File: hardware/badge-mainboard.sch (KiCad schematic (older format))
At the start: 35 parts, among them J1 Vin, J2 Vin, J3 Rpi_02x20_WaveShareEPD, J4 I2C_HEADER, J5 I2C_HEADER, SW1 User Button 2, SW2 User Button 1, SW3 User Button 3, SW4 User Button 4, U1 LM1117-3.3, U2 sensor-module-board

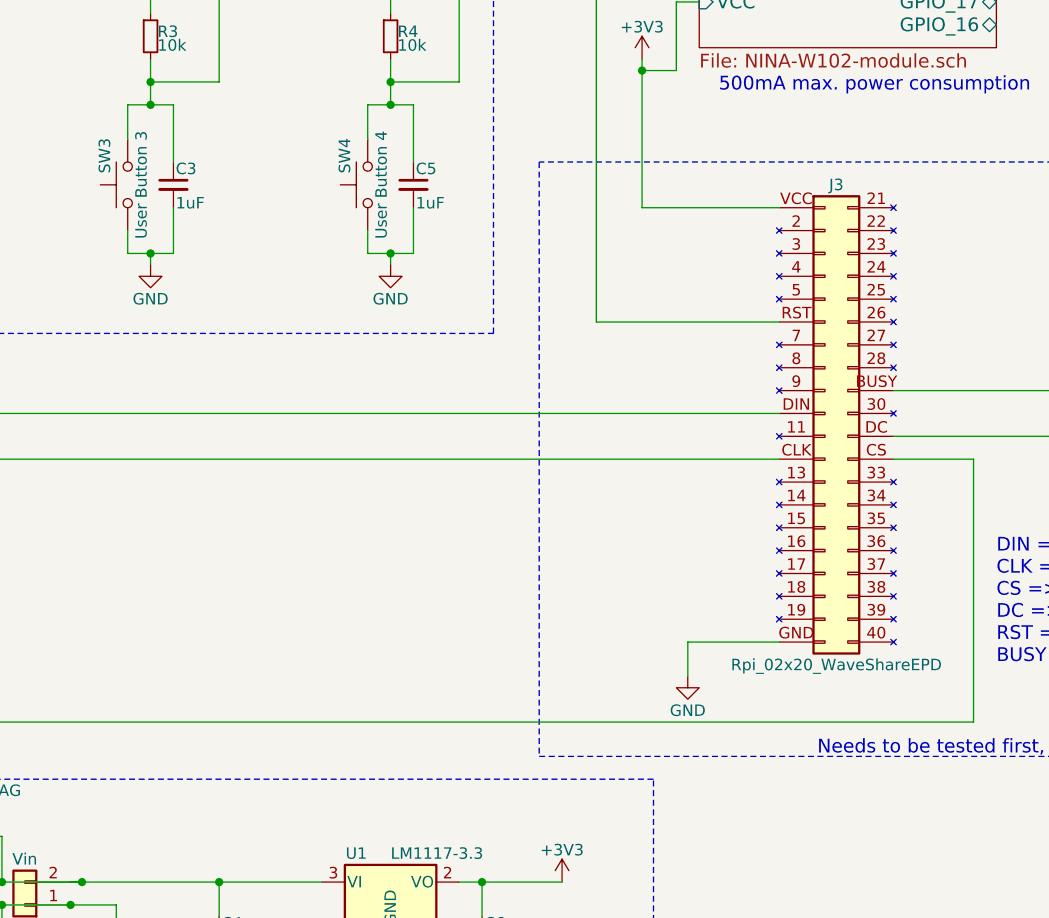
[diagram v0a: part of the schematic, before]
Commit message: Added some placement comments for the EPD to ensure orientation
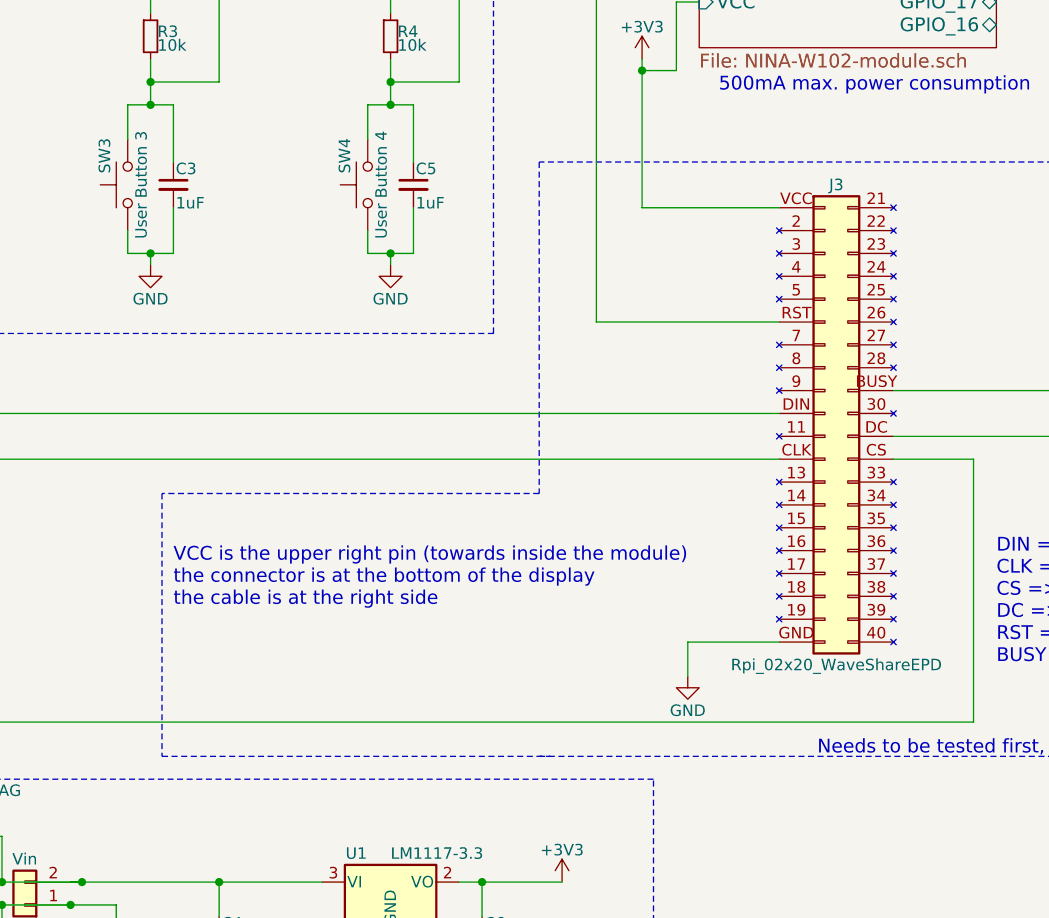
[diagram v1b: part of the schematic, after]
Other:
- note added: "VCC is the upper right pin (towards inside the module)\nthe connector is at the bottom of the display\nthe cable is at the right side"
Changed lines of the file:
@@
 	4750 5850 4750 6000
-Wire Notes Line
-	4100 3750 4100 6350
 Wire Notes Line
 	4100 6350 8700 6350
@@
 	4750 1250 4750 1200
 Connection ~ 4750 1200
+Text Notes 2500 5700 0    60   ~ 0
+VCC is the upper right pin (towards inside the module)\nthe connector is at the bottom of the display\nthe cable is at the right side
+Wire Notes Line
+	4100 5200 2450 5200
+Wire Notes Line
+	2450 5200 2450 6350
+Wire Notes Line
+	2450 6350 4150 6350
+Wire Notes Line
+	4100 3750 4100 5200
 $EndSCHEMATC

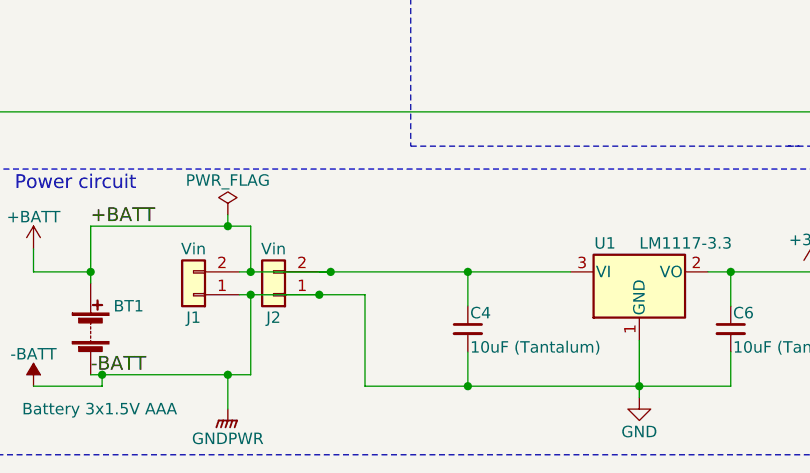
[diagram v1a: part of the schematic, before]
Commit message: removed duplicated battery terminal
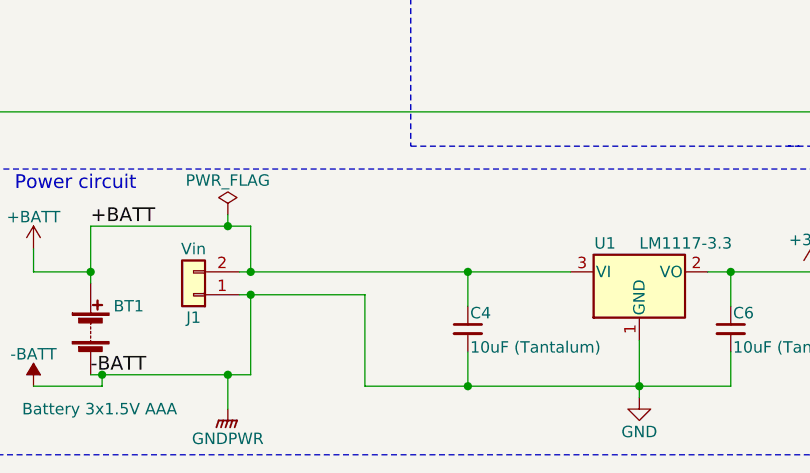
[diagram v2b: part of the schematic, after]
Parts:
- removed J2: Vin, symbol Conn_01x02
- BT1: footprint (none) -> Battery_Holders:Keystone_2479_3xAAA
- C1, C2, C3, C4, C5, C6, C7, C8, C9: footprint (none) -> Capacitors_SMD:C_1206
- D1: footprint (none) -> Diodes_SMD:D_SOD-123
- J1: footprint (none) -> Connectors-SparkFun:1X02_LOCK_LONGPADS
- J3: footprint (none) -> Connectors-SparkFun:2X20_NOSILK
- J4, J5: footprint (none) -> Connectors-SparkFun:1X04_LOCK_LONGPADS
- JP1: footprint SMT-JUMPER_2_NC -> lib:SMT-JUMPER_2_NC_TRACE_SILK
- LED1, LED2: footprint WS2812B_1 -> LED:WS2812B
- R1, R10, R2, R3, R4, R5, R6, R9: footprint (none) -> Resistors_SMD:R_1206
- R7, R8: footprint (none) -> Resistors_SMD:R_1206_HandSoldering
- SW1, SW2, SW3, SW4: footprint (none) -> switches:TACTILE_SWITCH_SMD_6.0X6.0MM
- U1: footprint (none) -> digikey-footprints:SOT-223
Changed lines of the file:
@@
 Title "IoT conference badge - mainboard"
 Date "2018-05-20"
-Rev "0.3.4"
+Rev "0.3.5"
 Comp "MakeZürich (makezurich.ch) & GDG Zürich (gdgzh.ch)"
 Comment1 ""
@@
 F 0 "LED1" H 10550 4300 50  0000 L CNN
 F 1 "WS2812b" H 10550 4200 50  0000 L CNN
-F 2 "WS2812B_1" H 10550 4100 50  0001 L CNN
+F 2 "LED:WS2812B" H 10550 4100 50  0001 L CNN
 F 3 "http://www.adafruit.com/datasheets/WS2812B.pdf" H 10550 4000 50  0001 L CNN
 F 4 "Intelligent control LED integrated light source, 4-pin SMD" H 10550 3900 50  0001 L CNN "Description"
@@
 F 0 "R5" H 7830 720 50  0000 L CNN
 F 1 "4.7k" H 7830 660 50  0000 L CNN
-F 2 "" H 7800 700 50  0001 C CNN
+F 2 "Resistors_SMD:R_1206" H 7800 700 50  0001 C CNN
 F 3 "" H 7800 700 50  0001 C CNN
 	1    7800 700
@@
 F 0 "C8" H 9360 4270 50  0000 L CNN
 F 1 "100nF" H 9360 4120 50  0000 L CNN
-F 2 "" H 9350 4200 50  0001 C CNN
+F 2 "Capacitors_SMD:C_1206" H 9350 4200 50  0001 C CNN
 F 3 "" H 9350 4200 50  0001 C CNN
 	1    9350 4200
@@
 F 0 "C9" H 9360 4920 50  0000 L CNN
 F 1 "100nF" H 9360 4770 50  0000 L CNN
-F 2 "" H 9350 4850 50  0001 C CNN
+F 2 "Capacitors_SMD:C_1206" H 9350 4850 50  0001 C CNN
 F 3 "" H 9350 4850 50  0001 C CNN
 	1    9350 4850
@@
 F 0 "C7" H 8960 4020 50  0000 L CNN
 F 1 "47uF" H 8960 3870 50  0000 L CNN
-F 2 "" H 8950 3950 50  0001 C CNN
+F 2 "Capacitors_SMD:C_1206" H 8950 3950 50  0001 C CNN
 F 3 "" H 8950 3950 50  0001 C CNN
 	1    8950 3950
@@
 F 0 "R6" H 7830 1270 50  0000 L CNN
 F 1 "4.7k" H 7830 1210 50  0000 L CNN
-F 2 "" H 7800 1250 50  0001 C CNN
+F 2 "Resistors_SMD:R_1206" H 7800 1250 50  0001 C CNN
 F 3 "" H 7800 1250 50  0001 C CNN
 	1    7800 1250
@@
 F 0 "J4" H 9250 2250 50  0000 C CNN
 F 1 "I2C_HEADER" H 9250 1750 50  0000 C CNN
-F 2 "" H 9250 2050 50  0001 C CNN
+F 2 "Connectors-SparkFun:1X04_LOCK_LONGPADS" H 9250 2050 50  0001 C CNN
 F 3 "" H 9250 2050 50  0001 C CNN
 	1    9250 2050
@@
 F 0 "J5" H 9800 2250 50  0000 C CNN
 F 1 "I2C_HEADER" H 9800 1750 50  0000 C CNN
-F 2 "" H 9800 2050 50  0001 C CNN
+F 2 "Connectors-SparkFun:1X04_LOCK_LONGPADS" H 9800 2050 50  0001 C CNN
 F 3 "" H 9800 2050 50  0001 C CNN
 	1    9800 2050
@@
 F 0 "R7" H 7830 1820 50  0000 L CNN
 F 1 "4.7k" H 7830 1760 50  0000 L CNN
-F 2 "" H 7800 1800 50  0001 C CNN
+F 2 "Resistors_SMD:R_1206_HandSoldering" H 7800 1800 50  0001 C CNN
 F 3 "" H 7800 1800 50  0001 C CNN
 	1    7800 1800
@@
 F 0 "R8" H 8180 1820 50  0000 L CNN
 F 1 "4.7k" H 8180 1760 50  0000 L CNN
-F 2 "" H 8150 1800 50  0001 C CNN
+F 2 "Resistors_SMD:R_1206_HandSoldering" H 8150 1800 50  0001 C CNN
 F 3 "" H 8150 1800 50  0001 C CNN
 	1    8150 1800
@@
 F 0 "U1" H 3300 7025 50  0000 C CNN
 F 1 "LM1117-3.3" H 3450 7025 50  0000 L CNN
-F 2 "" H 3450 6900 50  0001 C CNN
+F 2 "digikey-footprints:SOT-223" H 3450 6900 50  0001 C CNN
 F 3 "" H 3450 6900 50  0001 C CNN
 	1    3450 6900
@@
 F 0 "C4" H 2710 7220 50  0000 L CNN
 F 1 "10uF (Tantalum)" H 2710 7070 50  0000 L CNN
-F 2 "" H 2700 7150 50  0001 C CNN
+F 2 "Capacitors_SMD:C_1206" H 2700 7150 50  0001 C CNN
 F 3 "" H 2700 7150 50  0001 C CNN
 	1    2700 7150
@@
 F 0 "C6" H 3860 7220 50  0000 L CNN
 F 1 "10uF (Tantalum)" H 3860 7070 50  0000 L CNN
-F 2 "" H 3850 7150 50  0001 C CNN
+F 2 "Capacitors_SMD:C_1206" H 3850 7150 50  0001 C CNN
 F 3 "" H 3850 7150 50  0001 C CNN
 	1    3850 7150
@@
 $EndComp
 $Comp
-L Conn_01x02 J2
-U 1 1 5B02ACC9
-P 1850 7000
-F 0 "J2" H 1850 7100 50  0000 C CNN
-F 1 "Vin" H 1850 6800 50  0000 C CNN
-F 2 "" H 1850 7000 50  0001 C CNN
-F 3 "" H 1850 7000 50  0001 C CNN
-	1    1850 7000
-	-1   0    0    1
-$EndComp
-$Comp
 L Battery BT1
 U 1 1 5B02C983
@@
 F 0 "BT1" H 1150 7250 50  0000 L CNN
 F 1 "Battery 3x1.5V AAA" H 750 6800 50  0000 L CNN
-F 2 "" V 1050 7210 50  0001 C CNN
+F 2 "Battery_Holders:Keystone_2479_3xAAA" V 1050 7210 50  0001 C CNN
 F 3 "" V 1050 7210 50  0001 C CNN
 	1    1050 7150
@@
 F 0 "J1" H 1500 7100 50  0000 C CNN
 F 1 "Vin" H 1500 6800 50  0000 C CNN
-F 2 "" H 1500 7000 50  0001 C CNN
+F 2 "Connectors-SparkFun:1X02_LOCK_LONGPADS" H 1500 7000 50  0001 C CNN
 F 3 "" H 1500 7000 50  0001 C CNN
 	1    1500 7000
@@
 F 0 "LED2" H 10550 4900 50  0000 L CNN
 F 1 "WS2812b" H 10550 4800 50  0000 L CNN
-F 2 "WS2812B_1" H 10550 4700 50  0001 L CNN
+F 2 "LED:WS2812B" H 10550 4700 50  0001 L CNN
 F 3 "http://www.adafruit.com/datasheets/WS2812B.pdf" H 10550 4600 50  0001 L CNN
 F 4 "Intelligent control LED integrated light source, 4-pin SMD" H 10550 4500 50  0001 L CNN "Description"
@@
 F 0 "J3" H 5400 5850 50  0000 C CNN
 F 1 "Rpi_02x20_WaveShareEPD" H 5400 3750 50  0000 C CNN
-F 2 "" H 5350 4850 50  0001 C CNN
+F 2 "Connectors-SparkFun:2X20_NOSILK" H 5350 4850 50  0001 C CNN
 F 3 "" H 5350 4850 50  0001 C CNN
 	1    5350 4850
@@
 F 0 "SW2" H 1650 1700 50  0000 L CNN
 F 1 "User Button 1" H 1600 1540 50  0000 C CNN
-F 2 "" H 1600 1800 50  0001 C CNN
+F 2 "switches:TACTILE_SWITCH_SMD_6.0X6.0MM" H 1600 1800 50  0001 C CNN
 F 3 "" H 1600 1800 50  0001 C CNN
 	1    1600 1600
@@
 F 0 "C2" H 1810 1670 50  0000 L CNN
 F 1 "1uF" H 1810 1520 50  0000 L CNN
-F 2 "" H 1800 1600 50  0001 C CNN
+F 2 "Capacitors_SMD:C_1206" H 1800 1600 50  0001 C CNN
 F 3 "" H 1800 1600 50  0001 C CNN
 	1    1800 1600
@@
 F 0 "R2" H 1730 970 50  0000 L CNN
 F 1 "10k" H 1730 910 50  0000 L CNN
-F 2 "" H 1700 950 50  0001 C CNN
+F 2 "Resistors_SMD:R_1206" H 1700 950 50  0001 C CNN
 F 3 "" H 1700 950 50  0001 C CNN
 	1    1700 950
@@
 F 0 "SW1" H 1350 3950 50  0000 L CNN
 F 1 "User Button 2" H 1300 3790 50  0000 C CNN
-F 2 "" H 1300 4050 50  0001 C CNN
+F 2 "switches:TACTILE_SWITCH_SMD_6.0X6.0MM" H 1300 4050 50  0001 C CNN
 F 3 "" H 1300 4050 50  0001 C CNN
 	1    1300 3850
@@
 F 0 "C1" H 1510 3920 50  0000 L CNN
 F 1 "1uF" H 1510 3770 50  0000 L CNN
-F 2 "" H 1500 3850 50  0001 C CNN
+F 2 "Capacitors_SMD:C_1206" H 1500 3850 50  0001 C CNN
 F 3 "" H 1500 3850 50  0001 C CNN
 	1    1500 3850
@@
 F 0 "R1" H 1430 3220 50  0000 L CNN
 F 1 "10k" H 1430 3160 50  0000 L CNN
-F 2 "" H 1400 3200 50  0001 C CNN
+F 2 "Resistors_SMD:R_1206" H 1400 3200 50  0001 C CNN
 F 3 "" H 1400 3200 50  0001 C CNN
 	1    1400 3200
@@
 F 0 "SW3" H 2350 3950 50  0000 L CNN
 F 1 "User Button 3" H 2300 3790 50  0000 C CNN
-F 2 "" H 2300 4050 50  0001 C CNN
+F 2 "switches:TACTILE_SWITCH_SMD_6.0X6.0MM" H 2300 4050 50  0001 C CNN
 F 3 "" H 2300 4050 50  0001 C CNN
 	1    2300 3850
@@
 F 0 "C3" H 2510 3920 50  0000 L CNN
 F 1 "1uF" H 2510 3770 50  0000 L CNN
-F 2 "" H 2500 3850 50  0001 C CNN
+F 2 "Capacitors_SMD:C_1206" H 2500 3850 50  0001 C CNN
 F 3 "" H 2500 3850 50  0001 C CNN
 	1    2500 3850
@@
 F 0 "R3" H 2430 3220 50  0000 L CNN
 F 1 "10k" H 2430 3160 50  0000 L CNN
-F 2 "" H 2400 3200 50  0001 C CNN
+F 2 "Resistors_SMD:R_1206" H 2400 3200 50  0001 C CNN
 F 3 "" H 2400 3200 50  0001 C CNN
 	1    2400 3200
@@
 F 0 "SW4" H 3400 3950 50  0000 L CNN
 F 1 "User Button 4" H 3350 3790 50  0000 C CNN
-F 2 "" H 3350 4050 50  0001 C CNN
+F 2 "switches:TACTILE_SWITCH_SMD_6.0X6.0MM" H 3350 4050 50  0001 C CNN
 F 3 "" H 3350 4050 50  0001 C CNN
 	1    3350 3850
@@
 F 0 "C5" H 3560 3920 50  0000 L CNN
 F 1 "1uF" H 3560 3770 50  0000 L CNN
-F 2 "" H 3550 3850 50  0001 C CNN
+F 2 "Capacitors_SMD:C_1206" H 3550 3850 50  0001 C CNN
 F 3 "" H 3550 3850 50  0001 C CNN
 	1    3550 3850
@@
 F 0 "R4" H 3480 3220 50  0000 L CNN
 F 1 "10k" H 3480 3160 50  0000 L CNN
-F 2 "" H 3450 3200 50  0001 C CNN
+F 2 "Resistors_SMD:R_1206" H 3450 3200 50  0001 C CNN
 F 3 "" H 3450 3200 50  0001 C CNN
 	1    3450 3200
@@
 	3850 7400 3850 7250
 Wire Wire Line
-	2050 6900 3150 6900
-Wire Wire Line
 	2700 6900 2700 7050
 Connection ~ 2700 6900
@@
 Wire Wire Line
 	2250 7000 2250 7400
-Connection ~ 2050 7000
 Wire Wire Line
 	1050 6700 1050 6950
@@
 Connection ~ 1750 7000
 Wire Wire Line
-	1700 6900 2100 6900
-Connection ~ 2100 6900
+	1700 6900 3150 6900
 Wire Wire Line
 	1750 6900 1750 6700
@@
 F 0 "R9" H 4930 1220 50  0000 L CNN
 F 1 "100k" H 4930 1160 50  0000 L CNN
-F 2 "" H 4900 1200 50  0001 C CNN
+F 2 "Resistors_SMD:R_1206" H 4900 1200 50  0001 C CNN
 F 3 "" H 4900 1200 50  0001 C CNN
 	1    4900 1200
@@
 F 0 "R10" H 5530 1220 50  0000 L CNN
 F 1 "470k" H 5500 1100 50  0000 L CNN
-F 2 "" H 5500 1200 50  0001 C CNN
+F 2 "Resistors_SMD:R_1206" H 5500 1200 50  0001 C CNN
 F 3 "" H 5500 1200 50  0001 C CNN
 	1    5500 1200
@@
 F 0 "JP1" H 5700 1500 45  0000 L BNN
 F 1 "JUMPER-disable-batt-measurement" H 5000 1250 45  0000 L BNN
-F 2 "SMT-JUMPER_2_NC" H 5800 1600 20  0001 C CNN
+F 2 "lib:SMT-JUMPER_2_NC_TRACE_SILK" H 5800 1600 20  0001 C CNN
 F 3 "" H 5800 1400 60  0001 C CNN
 	1    5800 1400
@@
 F 0 "D1" H 4700 1350 50  0000 C CNN
 F 1 "D_Zener_3v3" H 4700 1550 50  0000 C CNN
-F 2 "" V 4700 1450 50  0001 C CNN
+F 2 "Diodes_SMD:D_SOD-123" V 4700 1450 50  0001 C CNN
 F 3 "" V 4700 1450 50  0001 C CNN
 	1    4700 1450

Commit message: Added footprints for modules
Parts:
- U2: footprint (none) -> badgeComponents:Sensors_module_board
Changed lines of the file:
@@
 F 0 "U2" H 8650 900 60  0000 C CNN
 F 1 "sensor-module-board" H 8650 750 60  0000 C CNN
-F 2 "" H 8650 900 60  0001 C CNN
+F 2 "badgeComponents:Sensors_module_board" H 8650 900 60  0001 C CNN
 F 3 "" H 8650 900 60  0001 C CNN
 	1    8650 900

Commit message: Initial netlist import and start of placing components
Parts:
- J1: footprint Connectors-SparkFun:1X02_LOCK_LONGPADS -> badgeComponents:VIN_1X02_LOCK_LONGPADS
- J3: footprint Connectors-SparkFun:2X20_NOSILK -> badgeComponents:Rpi_WaveShare_EPD_2X20_NOSILK
- J4, J5: footprint Connectors-SparkFun:1X04_LOCK_LONGPADS -> badgeComponents:I2C_HEADER_1X04_LOCK_LONGPADS
- JP1: footprint lib:SMT-JUMPER_2_NC_TRACE_SILK -> badgeComponents:SMT-JUMPER_2_NC_TRACE_SILK
- SW1, SW2, SW3, SW4: footprint switches:TACTILE_SWITCH_SMD_6.0X6.0MM -> badgeComponents:2-PIN-TACTILE_SWITCH_SMD_6.0X6.0MM
- U1: footprint digikey-footprints:SOT-223 -> badgeComponents:LM1117_SOT-223
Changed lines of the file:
@@
 F 0 "J4" H 9250 2250 50  0000 C CNN
 F 1 "I2C_HEADER" H 9250 1750 50  0000 C CNN
-F 2 "Connectors-SparkFun:1X04_LOCK_LONGPADS" H 9250 2050 50  0001 C CNN
+F 2 "badgeComponents:I2C_HEADER_1X04_LOCK_LONGPADS" H 9250 2050 50  0001 C CNN
 F 3 "" H 9250 2050 50  0001 C CNN
 	1    9250 2050
@@
 F 0 "J5" H 9800 2250 50  0000 C CNN
 F 1 "I2C_HEADER" H 9800 1750 50  0000 C CNN
-F 2 "Connectors-SparkFun:1X04_LOCK_LONGPADS" H 9800 2050 50  0001 C CNN
+F 2 "badgeComponents:I2C_HEADER_1X04_LOCK_LONGPADS" H 9800 2050 50  0001 C CNN
 F 3 "" H 9800 2050 50  0001 C CNN
 	1    9800 2050
@@
 F 0 "U1" H 3300 7025 50  0000 C CNN
 F 1 "LM1117-3.3" H 3450 7025 50  0000 L CNN
-F 2 "digikey-footprints:SOT-223" H 3450 6900 50  0001 C CNN
+F 2 "badgeComponents:LM1117_SOT-223" H 3450 6900 50  0001 C CNN
 F 3 "" H 3450 6900 50  0001 C CNN
 	1    3450 6900
@@
 F 0 "J1" H 1500 7100 50  0000 C CNN
 F 1 "Vin" H 1500 6800 50  0000 C CNN
-F 2 "Connectors-SparkFun:1X02_LOCK_LONGPADS" H 1500 7000 50  0001 C CNN
+F 2 "badgeComponents:VIN_1X02_LOCK_LONGPADS" H 1500 7000 50  0001 C CNN
 F 3 "" H 1500 7000 50  0001 C CNN
 	1    1500 7000
@@
 F 0 "J3" H 5400 5850 50  0000 C CNN
 F 1 "Rpi_02x20_WaveShareEPD" H 5400 3750 50  0000 C CNN
-F 2 "Connectors-SparkFun:2X20_NOSILK" H 5350 4850 50  0001 C CNN
+F 2 "badgeComponents:Rpi_WaveShare_EPD_2X20_NOSILK" H 5350 4850 50  0001 C CNN
 F 3 "" H 5350 4850 50  0001 C CNN
 	1    5350 4850
@@
 F 0 "SW2" H 1650 1700 50  0000 L CNN
 F 1 "User Button 1" H 1600 1540 50  0000 C CNN
-F 2 "switches:TACTILE_SWITCH_SMD_6.0X6.0MM" H 1600 1800 50  0001 C CNN
+F 2 "badgeComponents:2-PIN-TACTILE_SWITCH_SMD_6.0X6.0MM" H 1600 1800 50  0001 C CNN
 F 3 "" H 1600 1800 50  0001 C CNN
 	1    1600 1600
@@
 F 0 "SW1" H 1350 3950 50  0000 L CNN
 F 1 "User Button 2" H 1300 3790 50  0000 C CNN
-F 2 "switches:TACTILE_SWITCH_SMD_6.0X6.0MM" H 1300 4050 50  0001 C CNN
+F 2 "badgeComponents:2-PIN-TACTILE_SWITCH_SMD_6.0X6.0MM" H 1300 4050 50  0001 C CNN
 F 3 "" H 1300 4050 50  0001 C CNN
 	1    1300 3850
@@
 F 0 "SW3" H 2350 3950 50  0000 L CNN
 F 1 "User Button 3" H 2300 3790 50  0000 C CNN
-F 2 "switches:TACTILE_SWITCH_SMD_6.0X6.0MM" H 2300 4050 50  0001 C CNN
+F 2 "badgeComponents:2-PIN-TACTILE_SWITCH_SMD_6.0X6.0MM" H 2300 4050 50  0001 C CNN
 F 3 "" H 2300 4050 50  0001 C CNN
 	1    2300 3850
@@
 F 0 "SW4" H 3400 3950 50  0000 L CNN
 F 1 "User Button 4" H 3350 3790 50  0000 C CNN
-F 2 "switches:TACTILE_SWITCH_SMD_6.0X6.0MM" H 3350 4050 50  0001 C CNN
+F 2 "badgeComponents:2-PIN-TACTILE_SWITCH_SMD_6.0X6.0MM" H 3350 4050 50  0001 C CNN
 F 3 "" H 3350 4050 50  0001 C CNN
 	1    3350 3850
@@
 F 0 "JP1" H 5700 1500 45  0000 L BNN
 F 1 "JUMPER-disable-batt-measurement" H 5000 1250 45  0000 L BNN
-F 2 "lib:SMT-JUMPER_2_NC_TRACE_SILK" H 5800 1600 20  0001 C CNN
+F 2 "badgeComponents:SMT-JUMPER_2_NC_TRACE_SILK" H 5800 1600 20  0001 C CNN
 F 3 "" H 5800 1400 60  0001 C CNN
 	1    5800 1400
